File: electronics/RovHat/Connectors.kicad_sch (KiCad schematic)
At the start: 6 parts, among them J401 Conn_02x20_Odd_Even, J402 USB_A

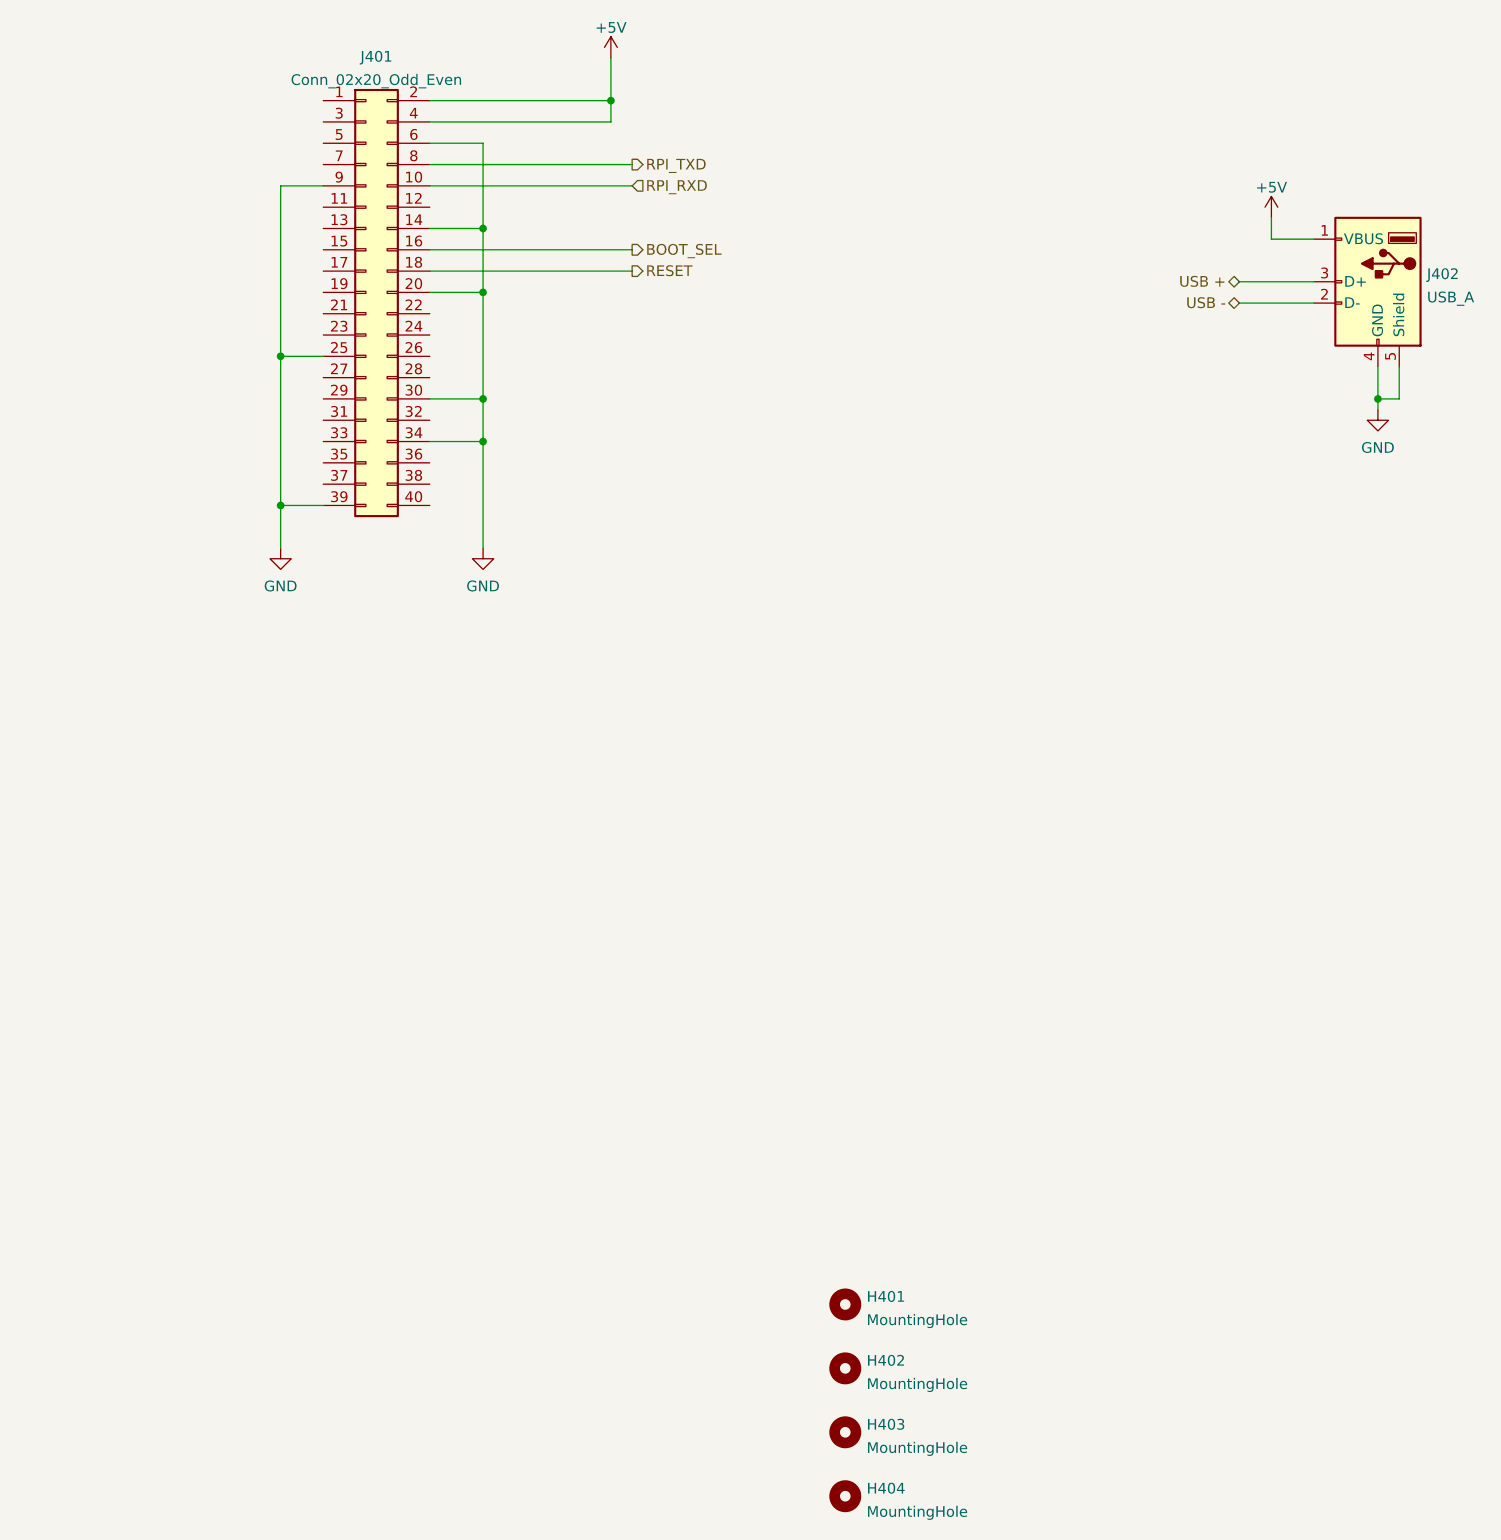
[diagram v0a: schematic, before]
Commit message: Changed To RPI Pico Module
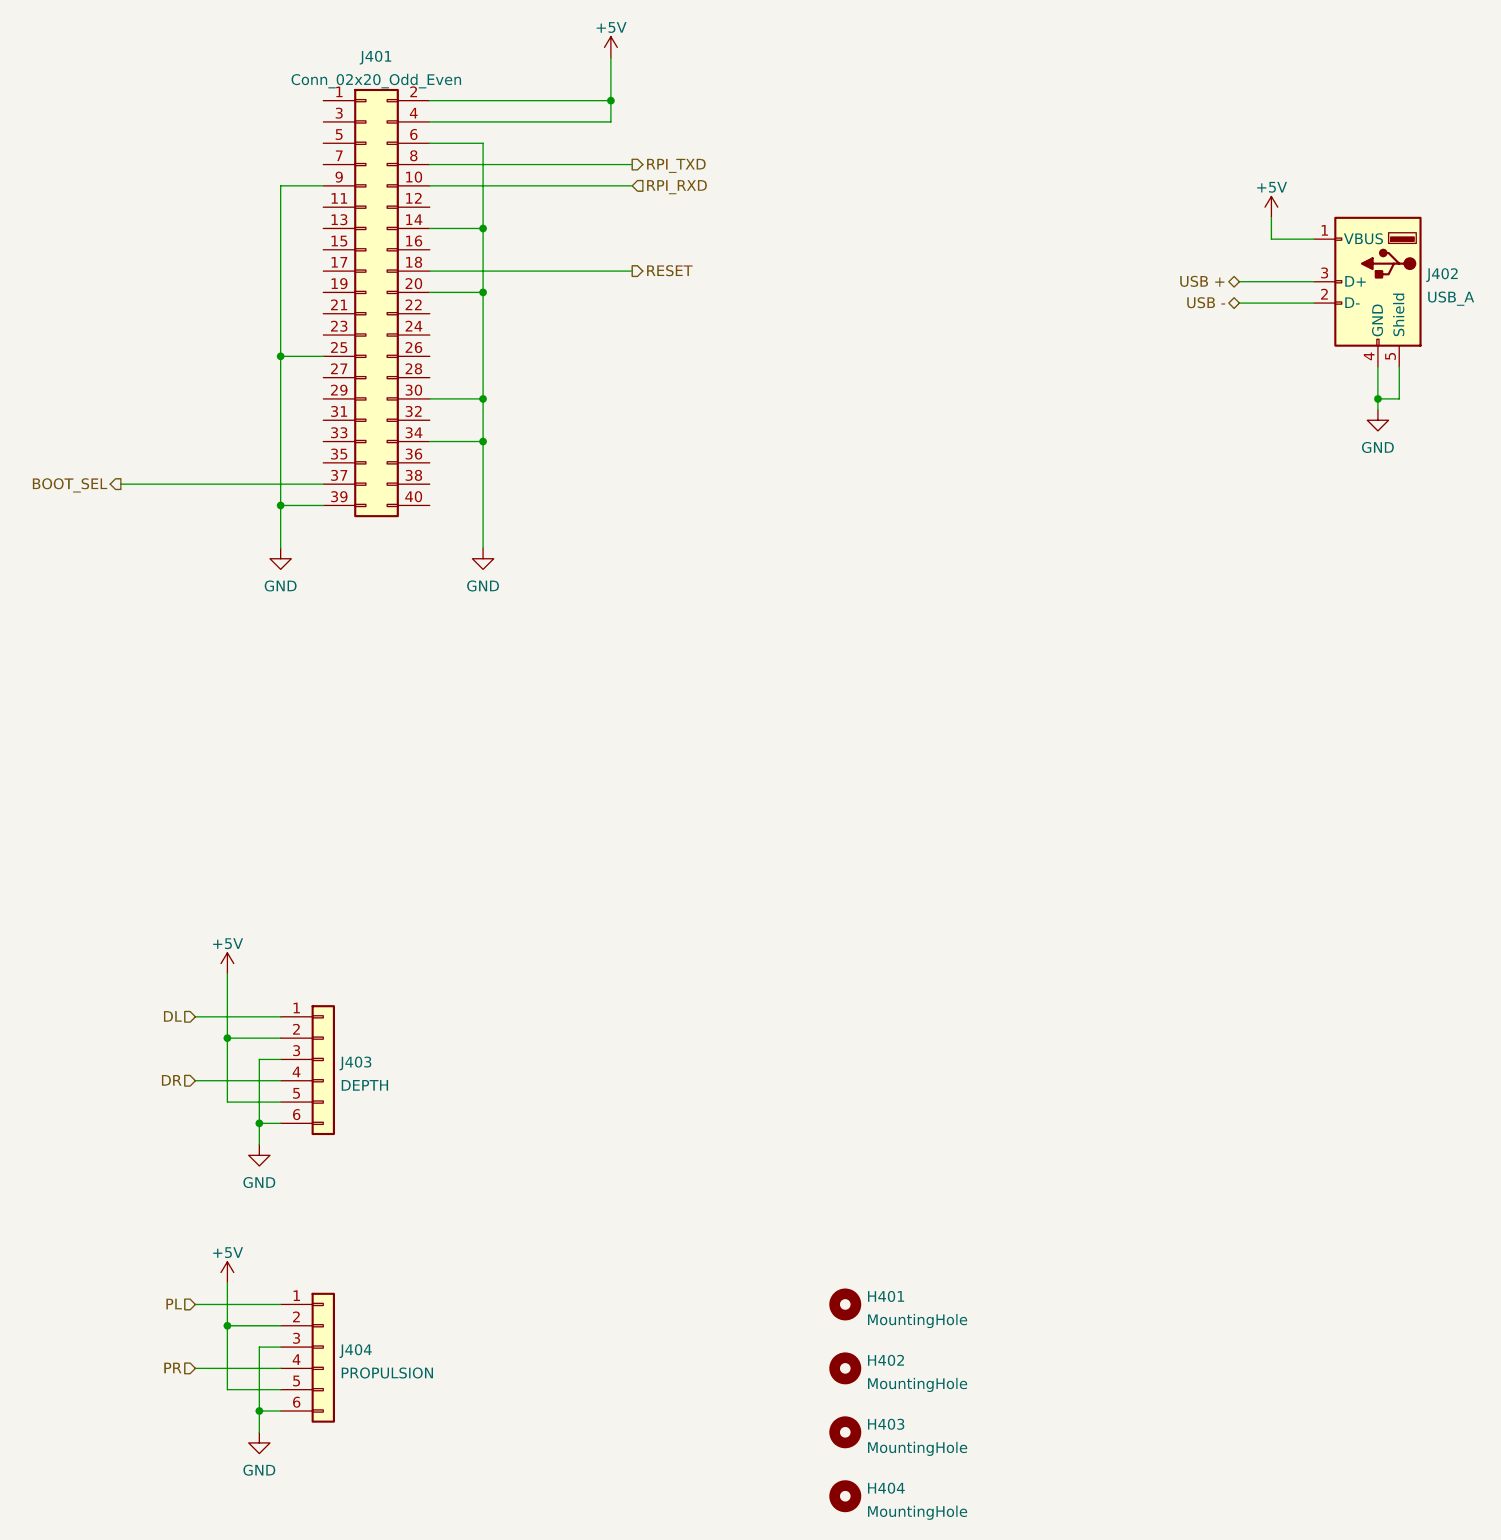
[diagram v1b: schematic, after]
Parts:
- added J403: DEPTH, Connector_PinHeader_2.54mm:PinHeader_1x06_P2.54mm_Vertical, symbol Connector_Generic:Conn_01x06
- added J404: PROPULSION, Connector_PinHeader_2.54mm:PinHeader_1x06_P2.54mm_Vertical, symbol Connector_Generic:Conn_01x06
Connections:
- net +5V: now also J403.2 (Pin_2), J403.5 (Pin_5), J404.2 (Pin_2), J404.5 (Pin_5)
- net BOOT_SEL: now also J401.37 (Pin_37); no longer J401.16 (Pin_16)
- net GND: now also J403.3 (Pin_3), J403.6 (Pin_6), J404.3 (Pin_3), J404.6 (Pin_6)
- new net DL: J403.1 (Pin_1)
- new net DR: J403.4 (Pin_4)
- new net PL: J404.1 (Pin_1)
- new net PR: J404.4 (Pin_4)

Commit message: Layout Done first level
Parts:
- J401: value Conn_02x20_Odd_Even -> RPI Header
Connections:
- net +5V: no longer J402.1 (VBUS)
- new net VBUS: J402.1 (VBUS)
- no-connect marks 0 -> 26
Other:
- moved on the sheet: J401

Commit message: Fabrication commit 2
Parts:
- removed H401, H402, H403, H404: MountingHole, MountingHole:MountingHole_2.7mm_M2.5, symbol Mechanical:MountingHole
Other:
- company: (none) -> Findersee
- title: (none) -> ROV RPI PICO HAT
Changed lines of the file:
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@@
 (kicad_sch (version 20211123) (generator eeschema)
   (paper "A4")
+  (title_block
+    (title "ROV RPI PICO HAT")
+    (date "2023-01-14")
+    (rev "1")
+    (company "Findersee")
+  )
   (junction (at 132.08 66.04) (diameter 0) (color 0 0 0 0)
   )
@@
     (data
       iVBORw0KGgoAAAANSUhEUgAAAxIAAAMOCAIAAAAFsqd8AAAAA3NCSVQICAjb4U/gAAAACXBIWXMA
-      AA6cAAAOnAEHlFPdAAAgAElEQVR4nOy9eXxU1d0/fu42+2SSAAkhEJC9bAq4V0TQQBVQQFyq1F3A
+      AA50AAAOdAFrJLPWAAAgAElEQVR4nOy9eXxU1d0/fu42+2SSAAkhEJC9bAq4V0TQQBVQQFyq1F3A
       tlrqWnGpqE9bq3WtintFAeWpKOICPrjwFQQUQUAQQXaIBEjIMtudufee3x/v3/28DpOFICSYeN5/
       5DWZOfds9yzv89mOwjlnEhISEhISEhISh4J6rCsgISEhISEhIdE8IGmThISEhISEhESDIGmThISE
@@
     (pin "6")
   )
-  (symbol (lib_id "Mechanical:MountingHole") (at 153.67 184.15 0) (unit 1)
-    (in_bom yes) (on_board yes) (fields_autoplaced)
-    (property "Reference" "H403" (id 0) (at 156.21 183.2415 0)
-      (effects (font (size 1.27 1.27)) (justify left))
-    )
-    (property "Value" "MountingHole" (id 1) (at 156.21 186.0166 0)
-      (effects (font (size 1.27 1.27)) (justify left))
-    )
-    (property "Footprint" "MountingHole:MountingHole_2.7mm_M2.5" (id 2) (at 153.67 184.15 0)
-      (effects (font (size 1.27 1.27)) hide)
-    )
-    (property "Datasheet" "~" (id 3) (at 153.67 184.15 0)
-      (effects (font (size 1.27 1.27)) hide)
-    )
-  )
   (symbol (lib_id "power:+5V") (at 80.01 166.37 0) (unit 1)
     (in_bom yes) (on_board yes) (fields_autoplaced)
@@
     (pin "1")
   )
-  (symbol (lib_id "Mechanical:MountingHole") (at 153.67 176.53 0) (unit 1)
-    (in_bom yes) (on_board yes) (fields_autoplaced)
-    (property "Reference" "H402" (id 0) (at 156.21 175.6215 0)
-      (effects (font (size 1.27 1.27)) (justify left))
-    )
-    (property "Value" "MountingHole" (id 1) (at 156.21 178.3966 0)
-      (effects (font (size 1.27 1.27)) (justify left))
-    )
-    (property "Footprint" "MountingHole:MountingHole_2.7mm_M2.5" (id 2) (at 153.67 176.53 0)
-      (effects (font (size 1.27 1.27)) hide)
-    )
-    (property "Datasheet" "~" (id 3) (at 153.67 176.53 0)
-      (effects (font (size 1.27 1.27)) hide)
-    )
-  )
   (symbol (lib_id "power:GND") (at 83.82 184.15 0) (unit 1)
     (in_bom yes) (on_board yes) (fields_autoplaced)
@@
     (pin "6")
   )
-  (symbol (lib_id "Mechanical:MountingHole") (at 153.67 168.91 0) (unit 1)
-    (in_bom yes) (on_board yes) (fields_autoplaced)
-    (property "Reference" "H401" (id 0) (at 156.21 168.0015 0)
-      (effects (font (size 1.27 1.27)) (justify left))
-    )
-    (property "Value" "MountingHole" (id 1) (at 156.21 170.7766 0)
-      (effects (font (size 1.27 1.27)) (justify left))
-    )
-    (property "Footprint" "MountingHole:MountingHole_2.7mm_M2.5" (id 2) (at 153.67 168.91 0)
-      (effects (font (size 1.27 1.27)) hide)
-    )
-    (property "Datasheet" "~" (id 3) (at 153.67 168.91 0)
-      (effects (font (size 1.27 1.27)) hide)
-    )
-  )
-  (symbol (lib_id "Mechanical:MountingHole") (at 153.67 191.77 0) (unit 1)
-    (in_bom yes) (on_board yes) (fields_autoplaced)
-    (property "Reference" "H404" (id 0) (at 156.21 190.8615 0)
-      (effects (font (size 1.27 1.27)) (justify left))
-    )
-    (property "Value" "MountingHole" (id 1) (at 156.21 193.6366 0)
-      (effects (font (size 1.27 1.27)) (justify left))
-    )
-    (property "Footprint" "MountingHole:MountingHole_2.7mm_M2.5" (id 2) (at 153.67 191.77 0)
-      (effects (font (size 1.27 1.27)) hide)
-    )
-    (property "Datasheet" "~" (id 3) (at 153.67 191.77 0)
-      (effects (font (size 1.27 1.27)) hide)
-    )
-  )
   (symbol (lib_id "Connector_Generic:Conn_02x20_Odd_Even") (at 118.11 48.26 0) (unit 1)

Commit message: Final Version
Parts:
- added R401, R402: 0R, Resistor_SMD:R_0603_1608Metric, symbol Device:R
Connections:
- net +5V: now also R401.2, R402.2; no longer J401.2 (Pin_2), J401.4 (Pin_4)
- new net: J401.2 (Pin_2), J401.4 (Pin_4), R401.1, R402.1
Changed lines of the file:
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@@
   (junction (at 132.08 48.26) (diameter 0) (color 0 0 0 0)
   )
+  (junction (at 132.08 27.94) (diameter 0) (color 0 0 0 0)
+  )
   (junction (at 217.17 60.96) (diameter 0) (color 0 0 0 0)
   )
@@
   (junction (at 107.95 73.66) (diameter 0) (color 0 0 0 0)
   )
-  (junction (at 147.32 25.4) (diameter 0) (color 0 0 0 0)
+  (junction (at 160.02 25.4) (diameter 0) (color 0 0 0 0)
   )
   (junction (at 132.08 60.96) (diameter 0) (color 0 0 0 0)
   )
+  (junction (at 132.08 25.4) (diameter 0) (color 0 0 0 0)
+  )
   (junction (at 107.95 55.88) (diameter 0) (color 0 0 0 0)
   )
@@
     (stroke (width 0) (type default) (color 0 0 0 0))
   )
+  (wire (pts (xy 132.08 25.4) (xy 132.08 27.94))
+    (stroke (width 0) (type default) (color 0 0 0 0))
+  )
   (wire (pts (xy 107.95 78.74) (xy 107.95 73.66))
     (stroke (width 0) (type default) (color 0 0 0 0))
@@
     (stroke (width 0) (type default) (color 0 0 0 0))
   )
+  (wire (pts (xy 139.7 25.4) (xy 132.08 25.4))
+    (stroke (width 0) (type default) (color 0 0 0 0))
+  )
   (wire (pts (xy 80.01 179.07) (xy 80.01 171.45))
     (stroke (width 0) (type default) (color 0 0 0 0))
@@
     (stroke (width 0) (type default) (color 0 0 0 0))
   )
-  (wire (pts (xy 125.73 25.4) (xy 147.32 25.4))
+  (wire (pts (xy 147.32 25.4) (xy 160.02 25.4))
     (stroke (width 0) (type default) (color 0 0 0 0))
   )
@@
     (stroke (width 0) (type default) (color 0 0 0 0))
   )
-  (wire (pts (xy 147.32 25.4) (xy 147.32 20.32))
+  (wire (pts (xy 160.02 25.4) (xy 160.02 20.32))
     (stroke (width 0) (type default) (color 0 0 0 0))
   )
@@
     (stroke (width 0) (type default) (color 0 0 0 0))
   )
-  (wire (pts (xy 125.73 27.94) (xy 147.32 27.94))
+  (wire (pts (xy 147.32 27.94) (xy 160.02 27.94))
     (stroke (width 0) (type default) (color 0 0 0 0))
   )
@@
     (stroke (width 0) (type default) (color 0 0 0 0))
   )
+  (wire (pts (xy 132.08 25.4) (xy 125.73 25.4))
+    (stroke (width 0) (type default) (color 0 0 0 0))
+  )
   (wire (pts (xy 113.03 71.12) (xy 104.14 71.12))
     (stroke (width 0) (type default) (color 0 0 0 0))
@@
     (stroke (width 0) (type default) (color 0 0 0 0))
   )
+  (wire (pts (xy 139.7 27.94) (xy 132.08 27.94))
+    (stroke (width 0) (type default) (color 0 0 0 0))
+  )
   (wire (pts (xy 200.66 46.99) (xy 209.55 46.99))
     (stroke (width 0) (type default) (color 0 0 0 0))
@@
     (stroke (width 0) (type default) (color 0 0 0 0))
   )
+  (wire (pts (xy 132.08 27.94) (xy 125.73 27.94))
+    (stroke (width 0) (type default) (color 0 0 0 0))
+  )
   (wire (pts (xy 125.73 60.96) (xy 132.08 60.96))
     (stroke (width 0) (type default) (color 0 0 0 0))
   )
-  (wire (pts (xy 147.32 27.94) (xy 147.32 25.4))
+  (wire (pts (xy 160.02 27.94) (xy 160.02 25.4))
     (stroke (width 0) (type default) (color 0 0 0 0))
   )
@@
     (pin "1")
   )
-  (symbol (lib_id "power:+5V") (at 147.32 20.32 0) (unit 1)
+  (symbol (lib_id "power:+5V") (at 160.02 20.32 0) (unit 1)
+    (in_bom yes) (on_board yes)
+    (property "Reference" "#PWR0403" (id 0) (at 160.02 24.13 0)
+      (effects (font (size 1.27 1.27)) hide)
+    )
+    (property "Value" "+5V" (id 1) (at 160.02 16.7155 0))
+    (property "Footprint" "" (id 2) (at 160.02 20.32 0)
+      (effects (font (size 1.27 1.27)) hide)
+    )
+    (property "Datasheet" "" (id 3) (at 160.02 20.32 0)
+      (effects (font (size 1.27 1.27)) hide)
+    )
+    (pin "1")
+  )
+  (symbol (lib_id "Device:R") (at 143.51 27.94 90) (mirror x) (unit 1)
     (in_bom yes) (on_board yes)
-    (property "Reference" "#PWR0403" (id 0) (at 147.32 24.13 0)
+    (property "Reference" "R402" (id 0) (at 147.32 26.67 90)
+      (effects (font (size 1.27 1.27)) (justify right))
+    )
+    (property "Value" "0R" (id 1) (at 143.51 27.94 90))
+    (property "Footprint" "Resistor_SMD:R_0603_1608Metric" (id 2) (at 143.51 26.162 90)
       (effects (font (size 1.27 1.27)) hide)
     )
-    (property "Value" "+5V" (id 1) (at 147.32 16.7155 0))
-    (property "Footprint" "" (id 2) (at 147.32 20.32 0)
+    (property "Datasheet" "~" (id 3) (at 143.51 27.94 0)
       (effects (font (size 1.27 1.27)) hide)
     )
-    (property "Datasheet" "" (id 3) (at 147.32 20.32 0)
+    (pin "1")
+    (pin "2")
+  )
+  (symbol (lib_id "Device:R") (at 143.51 25.4 90) (mirror x) (unit 1)
+    (in_bom yes) (on_board yes)
+    (property "Reference" "R401" (id 0) (at 147.32 24.13 90)
+      (effects (font (size 1.27 1.27)) (justify right))
+    )
+    (property "Value" "0R" (id 1) (at 143.51 25.4 90))
+    (property "Footprint" "Resistor_SMD:R_0603_1608Metric" (id 2) (at 143.51 23.622 90)
+      (effects (font (size 1.27 1.27)) hide)
+    )
+    (property "Datasheet" "~" (id 3) (at 143.51 25.4 0)
       (effects (font (size 1.27 1.27)) hide)
     )
     (pin "1")
+    (pin "2")
   )
   (symbol (lib_id "power:GND") (at 107.95 78.74 0) (unit 1)
